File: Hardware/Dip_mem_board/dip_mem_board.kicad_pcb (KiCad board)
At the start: 4 copper layers, 52.5 x 20 mm, 10 parts, among them P1 CONN_01X20, P2 CONN_01X20, U1 SN74LVC4245A, U2 SN74LVC4245A, U3 39VF1681-70EKE, U4 SN74LVC4245A, U5 TLV70033DDC, U6 SN74LVC4245A

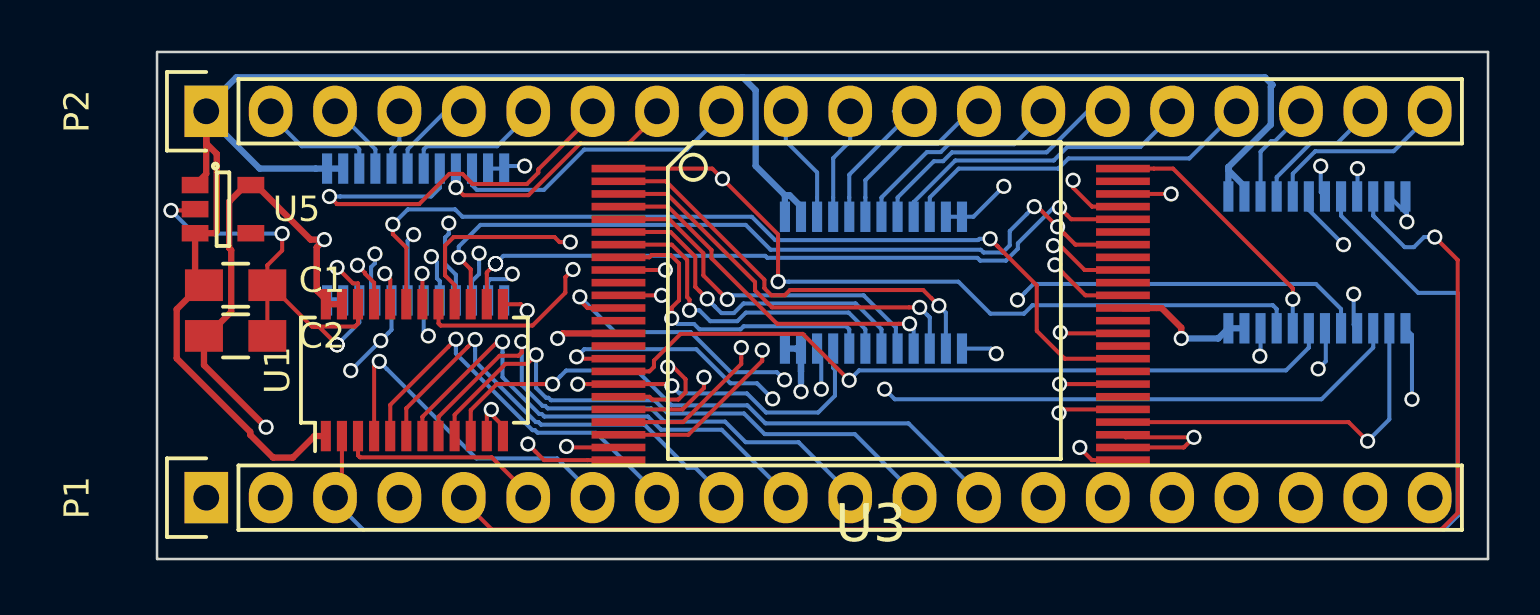
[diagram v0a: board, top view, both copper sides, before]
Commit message: Schematic ERC corrections
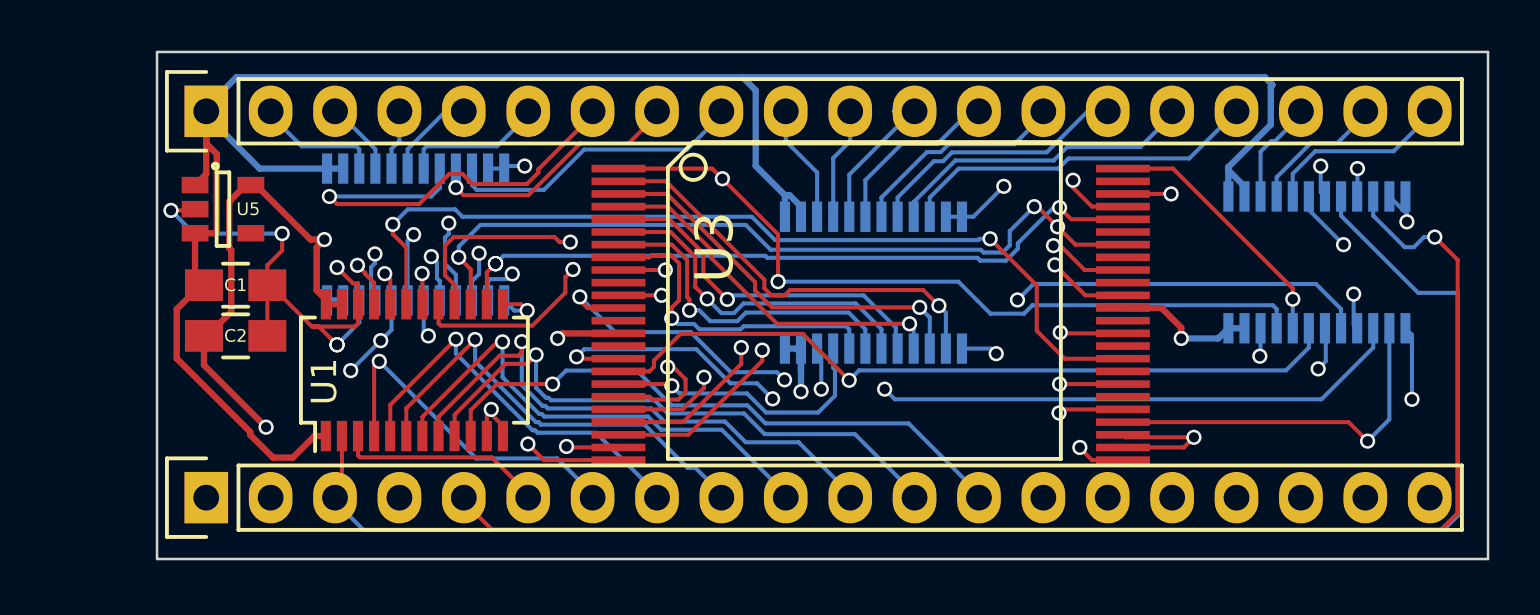
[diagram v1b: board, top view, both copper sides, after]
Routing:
- net /A8: track 12.8 -> 11.2 mm, vias 2 -> 1
- net +3V3: track 83.2 -> 82.1 mm
- net GND: track 139.1 -> 140.1 mm
